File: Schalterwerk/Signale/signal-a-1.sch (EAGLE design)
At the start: 29 parts, among them Q1 NPN-23, Q2 NPN-23, Q3 NPN-23, Q4 NPN-23, X1 PHNX_4P_508CONN_1017493, X2 PHNX_4P_508CONN_1017493, X3 PHNX_4P_350CONN_1984989_PXC, X4 PHNX_4P_350CONN_1984989_PXC, X5 RJ45-JACK

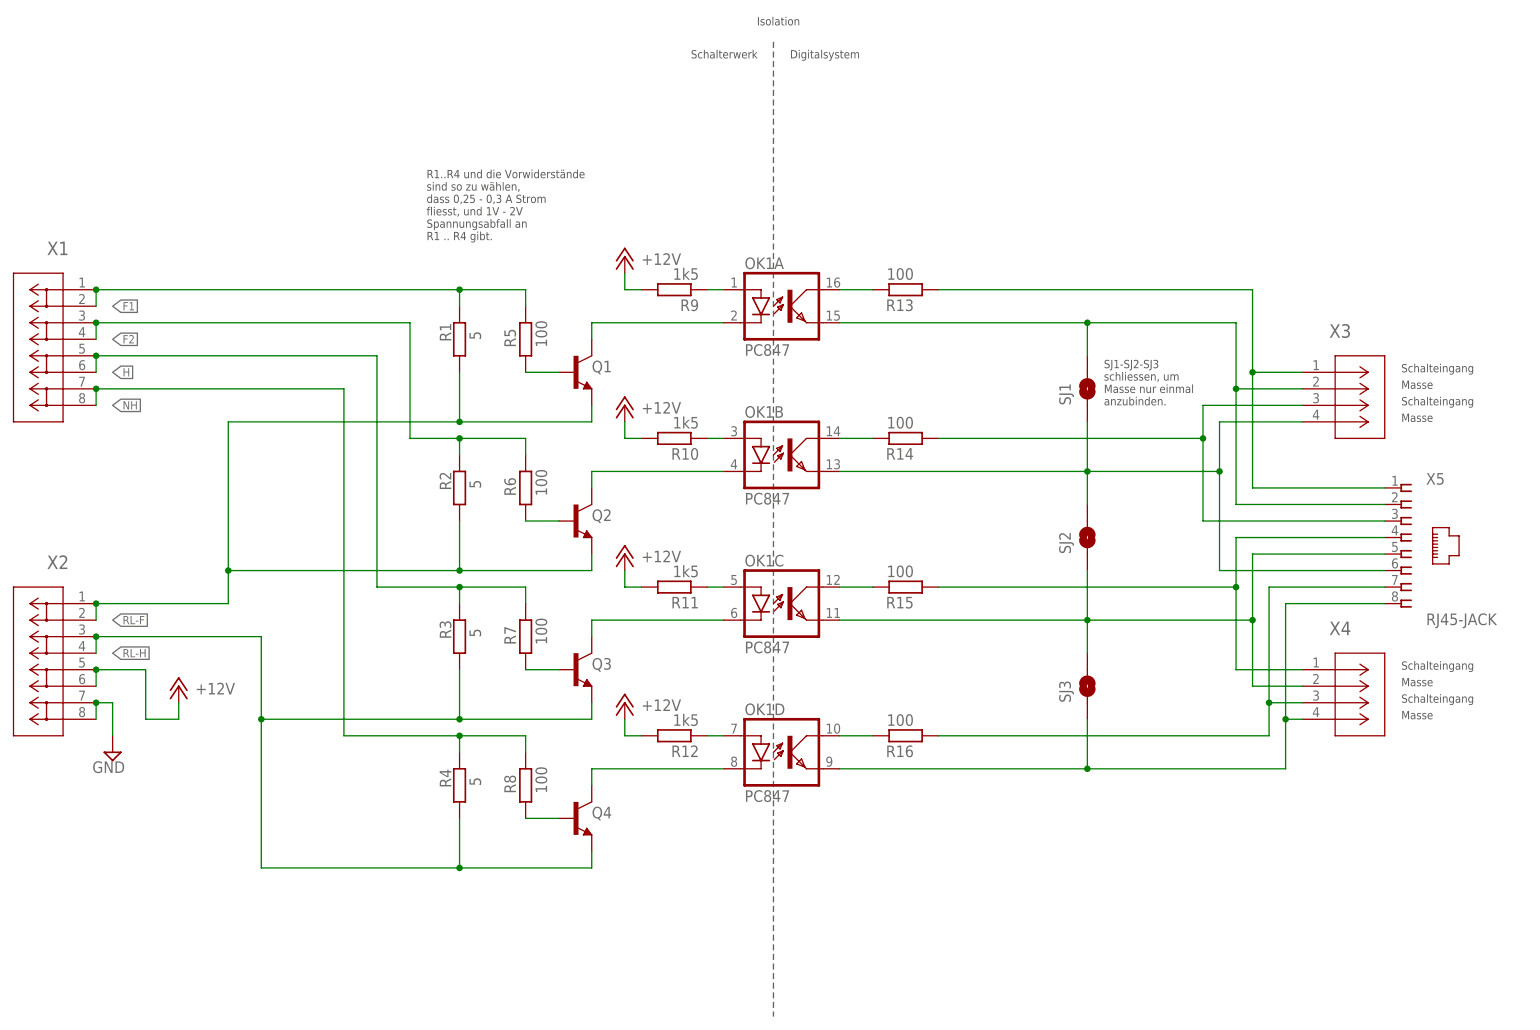
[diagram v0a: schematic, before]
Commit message: Updates the frames on the schematics with proper project information.
Adds LEDs for observing what is happening on the Gleisbelegtmeldung.
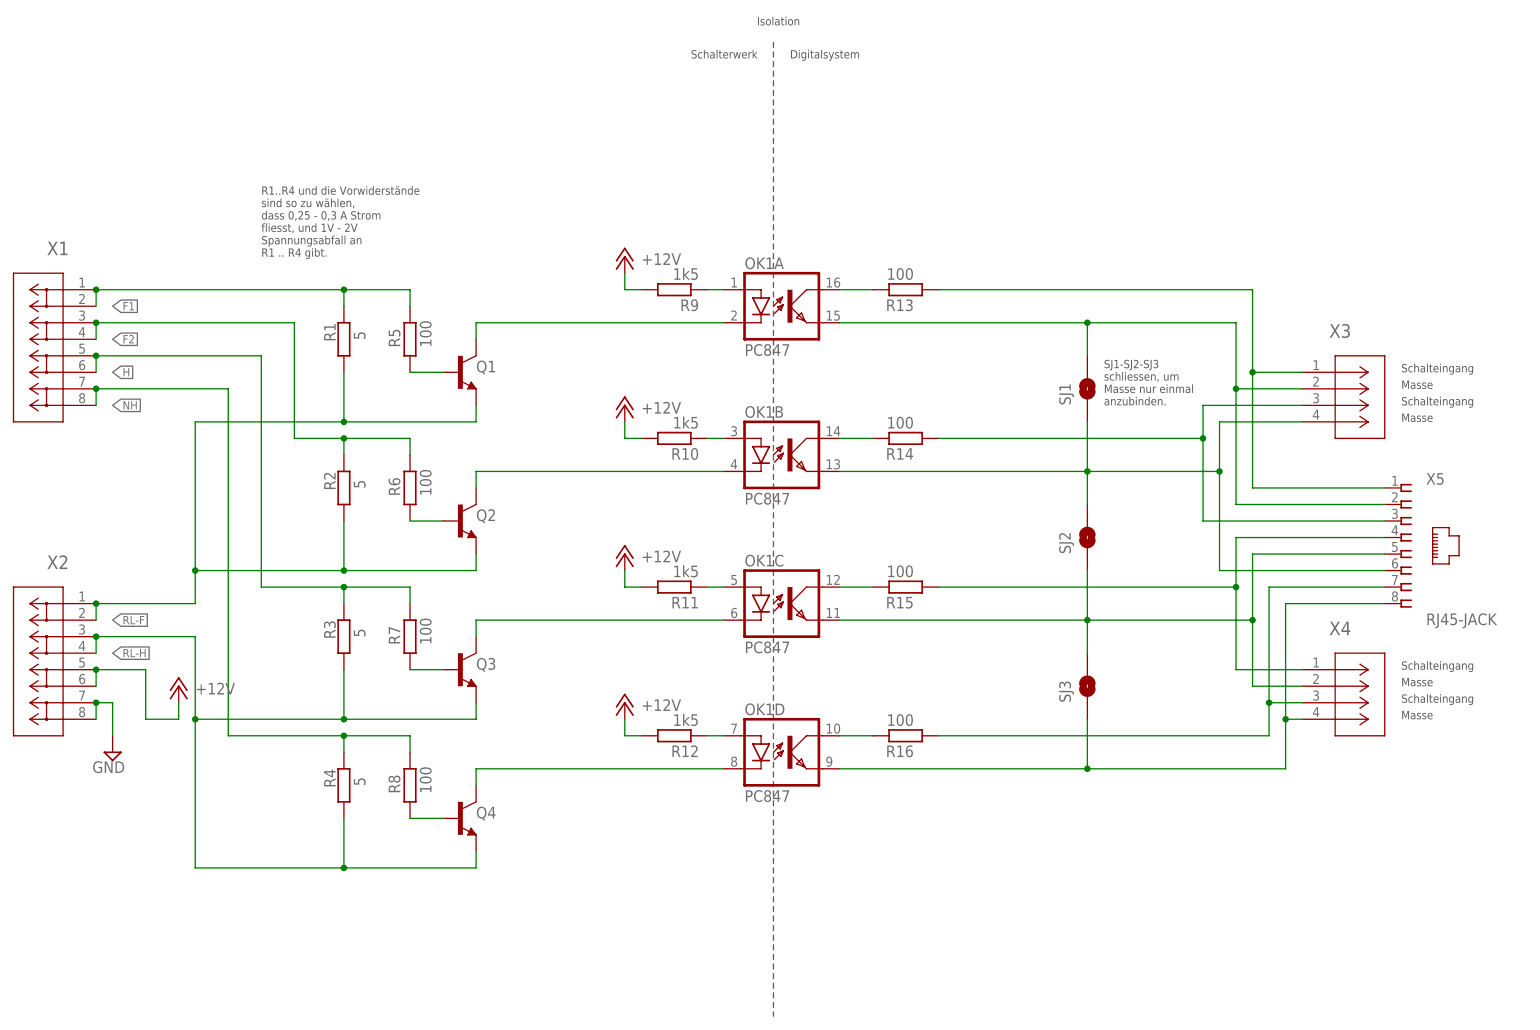
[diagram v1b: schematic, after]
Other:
- moved on the sheet: Q1, Q2, Q3, Q4, R1, R2, R3, R4, R5, R6, R7, R8

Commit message: Adds LED.
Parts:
- added D1: (no value), led:LEDCHIPLED_0603
- added R17: 1k5, rcl:R-EU_R0805
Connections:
- new net GND1: D1.C
- new net N$24: R17.2
- new net N$25: D1.A, R17.1
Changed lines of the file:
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@@
 <part name="SJ2" library="eagleparts" deviceset="SJ" device="RND2"/>
 <part name="SJ3" library="eagleparts" deviceset="SJ" device="RND2"/>
+<part name="D1" library="led" library_urn="urn:adsk.eagle:library:259" deviceset="LED" device="CHIPLED_0603" package3d_urn="urn:adsk.eagle:package:15822/2"/>
+<part name="R17" library="rcl" library_urn="urn:adsk.eagle:library:334" deviceset="R-EU_" device="R0805" package3d_urn="urn:adsk.eagle:package:23553/2" value="1k5"/>
 </parts>
 <sheets>
@@
 <attribute name="VALUE" x="189.23" y="78.74" size="1.778" layer="96" rot="R90"/>
 </instance>
+<instance part="D1" gate="G$1" x="106.68" y="154.94" smashed="yes" rot="R90">
+<attribute name="NAME" x="111.252" y="158.496" size="1.778" layer="95" rot="R180"/>
+<attribute name="VALUE" x="111.252" y="160.655" size="1.778" layer="96" rot="R180"/>
+</instance>
+<instance part="R17" gate="G$1" x="96.52" y="154.94" smashed="yes" rot="R180">
+<attribute name="NAME" x="100.33" y="153.4414" size="1.778" layer="95" rot="R180"/>
+<attribute name="VALUE" x="100.33" y="158.242" size="1.778" layer="96" rot="R180"/>
+</instance>
 </instances>
 <busses>
@@
 </segment>
 </net>
+<net name="N$24" class="0">
+<segment>
+<pinref part="R17" gate="G$1" pin="2"/>
+<wire x1="88.9" y1="154.94" x2="91.44" y2="154.94" width="0.1524" layer="91"/>
+</segment>
+</net>
+<net name="GND1" class="0">
+<segment>
+<pinref part="D1" gate="G$1" pin="C"/>
+<wire x1="111.76" y1="154.94" x2="116.84" y2="154.94" width="0.1524" layer="91"/>
+</segment>
+</net>
+<net name="N$25" class="0">
+<segment>
+<pinref part="R17" gate="G$1" pin="1"/>
+<pinref part="D1" gate="G$1" pin="A"/>
+<wire x1="101.6" y1="154.94" x2="104.14" y2="154.94" width="0.1524" layer="91"/>
+</segment>
+</net>
